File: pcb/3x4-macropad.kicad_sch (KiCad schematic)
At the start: 47 parts, among them SW1 SW_Push, SW10 SW_Push, SW11 SW_Push, SW12 SW_Push, SW2 SW_Push, SW3 SW_Push, SW4 SW_Push, SW5 SW_Push, SW6 SW_Push, SW7 SW_Push, SW8 SW_Push, SW9 SW_Push, U1 WeAct-RP2040-Pico

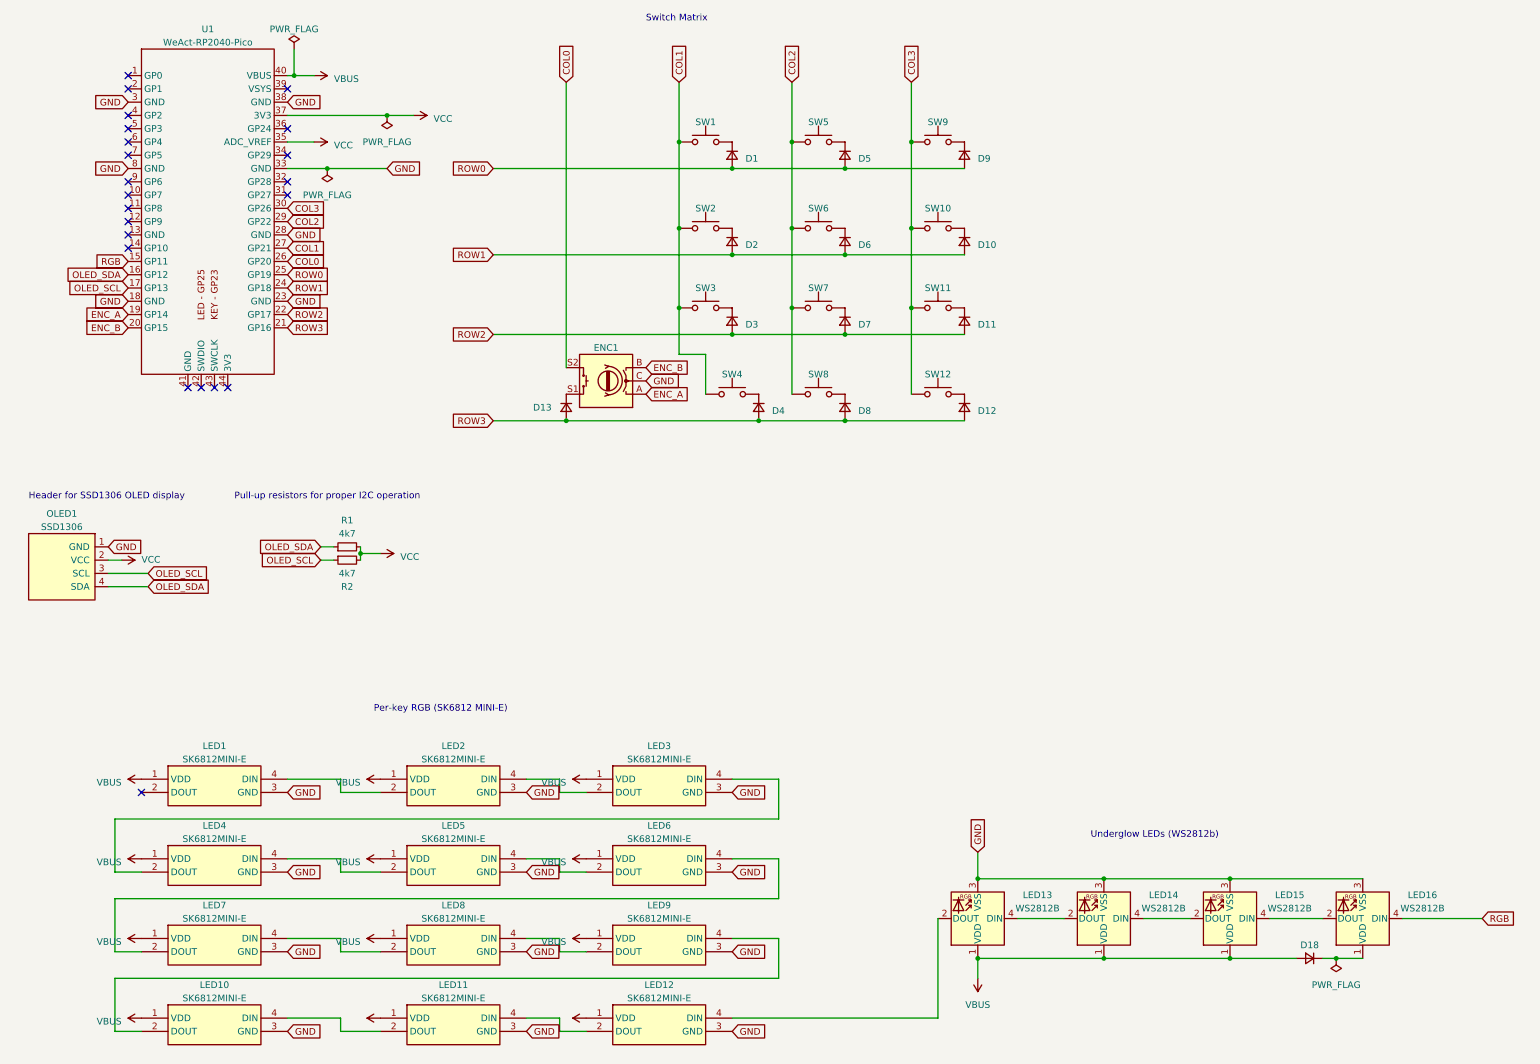
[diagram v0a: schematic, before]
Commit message: stuff
- cleaned up routing
- changed per-key rgb footprint
- changed resistor footprint
- changed diode footprint to actually support sod123
- made power traces 0.5mm
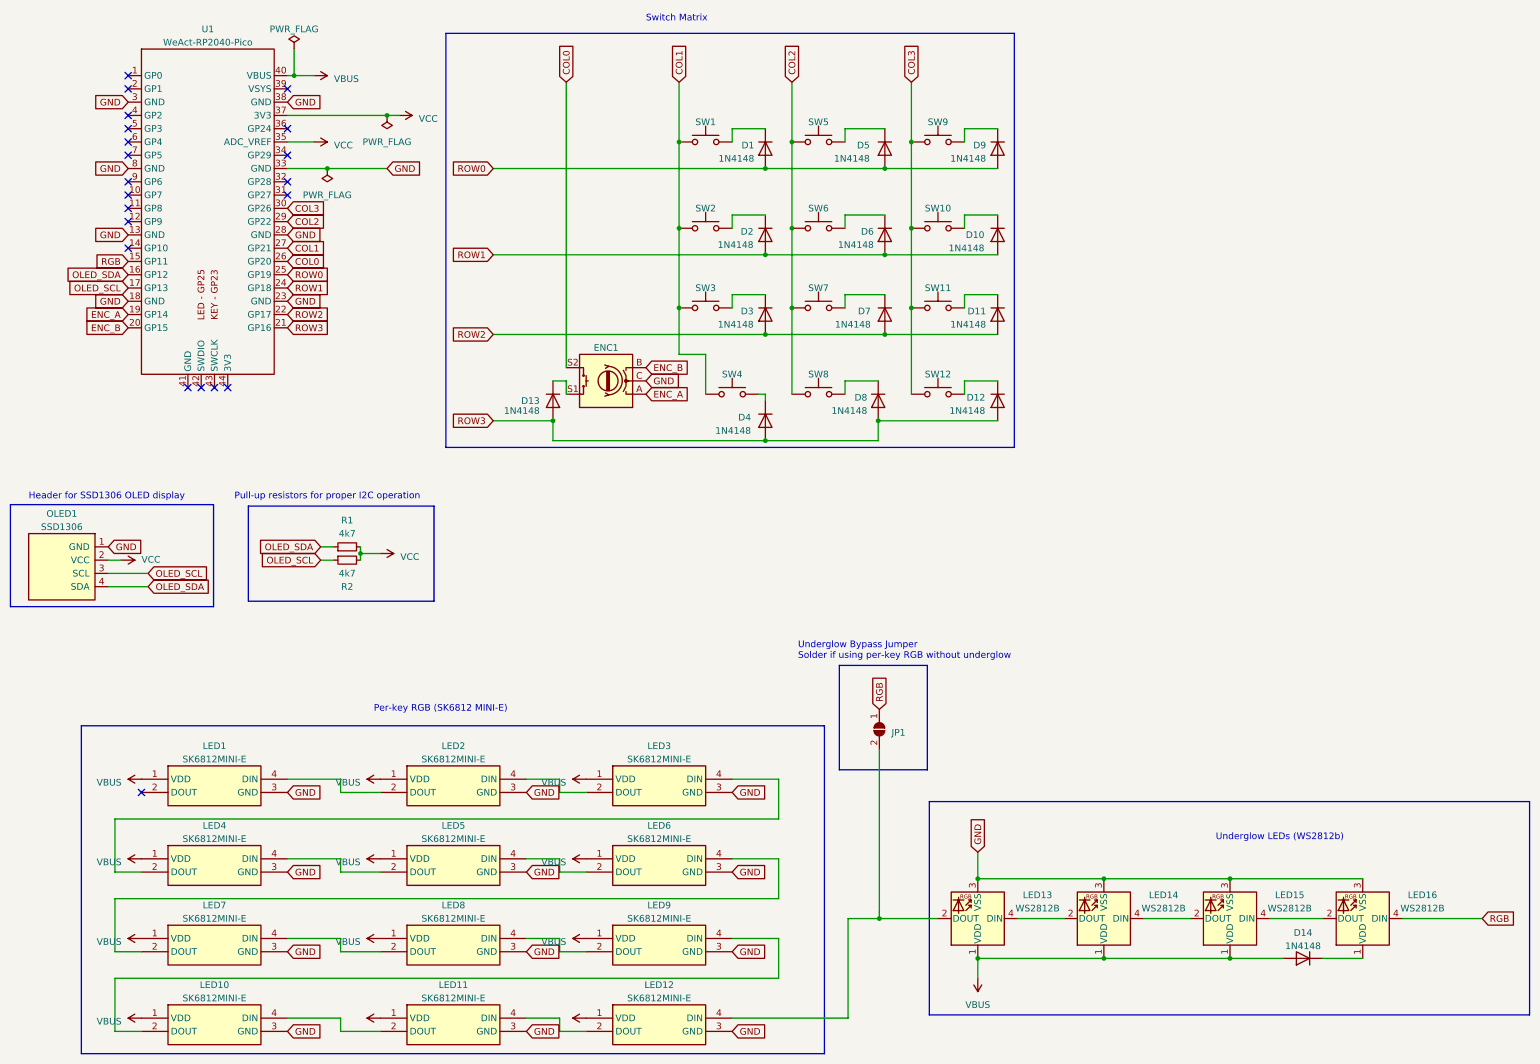
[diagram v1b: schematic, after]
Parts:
- removed D1, D10, D11, D12, D13, D18, D2, D3, D4, D5, D6, D7, D8, D9: D_Small, Keebio-Parts:Diode-dual, symbol Device:D_Small
- added D1, D10, D11, D12, D13, D14, D2, D3, D4, D5, D6, D7, D8, D9: 1N4148, Keebio-Parts:Diode-Hybrid-Back, symbol Diode:1N4148
- added JP1: SolderJumper_2_Open, Jumper:SolderJumper-2_P1.3mm_Open_RoundedPad1.0x1.5mm, symbol Jumper:SolderJumper_2_Open
- LED1, LED10, LED11, LED12, LED2, LED3, LED4, LED5, LED6, LED7, LED8, LED9: footprint SK6812MINI-E:SK6812MINIE -> Keebio-Parts:SK6812-MINI-E
- LED13, LED14, LED15, LED16: footprint LED_SMD:LED_WS2812B_PLCC4_5.0x5.0mm_P3.2mm -> Keebio-Parts:WS2812B
- R1, R2: footprint Resistor_THT:R_Axial_DIN0204_L3.6mm_D1.6mm_P5.08mm_Horizontal -> Keebio-Parts:Resistor-Hybrid
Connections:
- net GND: now also U1.13 (GND)
- net RGB: now also JP1.1 (A)
- net ROW0: now also D1.2 (A), D5.2 (A), D9.2 (A)
- net ROW1: now also D10.2 (A), D2.2 (A), D6.2 (A)
- net ROW2: now also D11.2 (A), D3.2 (A), D7.2 (A)
- net ROW3: now also D12.2 (A), D13.2 (A), D4.2 (A), D8.2 (A)
- net VBUS: now also D14.2 (A)
- net at SW10.2: now also D10.1 (K)
- net at SW6.2: now also D6.1 (K)
- net at SW12.2: now also D12.1 (K)
- net at SW1.2: now also D1.1 (K)
- net at SW3.2: now also D3.1 (K)
- net at SW5.2: now also D5.1 (K)
- net at SW7.2: now also D7.1 (K)
- net at SW2.2: now also D2.1 (K)
- net at SW11.2: now also D11.1 (K)
- net at SW4.2: now also D4.1 (K)
- net at SW9.2: now also D9.1 (K)
- net at LED16.1 (VDD): now also D14.1 (K)
- net at LED12.4 (DIN), LED13.2 (DOUT): now also JP1.2 (B)
- net at ENC1.S1: now also D13.1 (K)
- net at SW8.2: now also D8.1 (K)
- no-connect marks 22 -> 21
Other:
- note added: "Underglow Bypass Jumper Solder if using per-key RGB without underglow"

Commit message: Init rp2040 on board
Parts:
- removed U1: WeAct-RP2040-Pico, WeAct-RP2040-Pico:WeAct-RP2040-Pico, symbol WeAct-RP2040-Pico:WeAct-RP2040-Pico
- added C1, C16: 10u, Capacitor_SMD:C_0805_2012Metric, symbol Device:C_Small
- added C10, C2: 1u, Capacitor_SMD:C_0402_1005Metric, symbol Device:C_Small
- added C11, C12, C13, C3, C4, C5, C6, C7, C8, C9: 100n, Capacitor_SMD:C_0402_1005Metric, symbol Device:C_Small
- added C14, C15: 27pF, Capacitor_SMD:C_0402_1005Metric, symbol Device:C_Small
- added J2: Conn_01x02, Keebio-Parts:SW_Tactile_SPST_Angled_MJTP1117, symbol Connector_Generic:Conn_01x02
- added J3: Conn_01x02, Connector_PinHeader_1.00mm:PinHeader_1x02_P1.00mm_Vertical, symbol Connector_Generic:Conn_01x02
- added J4: USB_C_Receptacle_USB2.0, Connector_USB:USB_C_Receptacle_HRO_TYPE-C-31-M-12, symbol Connector:USB_C_Receptacle_USB2.0
- added R10, R7, R9: 1k, Resistor_SMD:R_0402_1005Metric, symbol Device:R_Small
- added R3, R4: 5k1, Resistor_SMD:R_0805_2012Metric, symbol Device:R_Small
- added R5, R6: 27.4, Resistor_SMD:R_0402_1005Metric, symbol Device:R_Small
- added R8: DNF(10k), Resistor_SMD:R_0402_1005Metric, symbol Device:R_Small
- added U1: RP2040, RP2040_minimal:RP2040-QFN-56, symbol MCU_RaspberryPi_RP2040:RP2040
- added U2: NCP1117-3.3_SOT223, Package_TO_SOT_SMD:SOT-223-3_TabPin2, symbol Regulator_Linear:NCP1117-3.3_SOT223
- added U3: W25Q32JVSS, Package_SO:SOIC-8_5.23x5.23mm_P1.27mm, symbol Memory_Flash:W25Q32JVSS
- added Y1: ABLS_12.000MHZ-B4-T, RP2040_minimal:Crystal_SMD_HC49-US, symbol Device:Crystal_Small
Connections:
- net COL0: now also U1.31 (GPIO20)
- net COL1: now also U1.32 (GPIO21)
- net COL2: now also U1.34 (GPIO22)
- net COL3: now also U1.38 (GPIO26_ADC0)
- net ENC_A: now also U1.17 (GPIO14)
- net ENC_B: now also U1.18 (GPIO15)
- net OLED_SCL: now also U1.16 (GPIO13)
- net OLED_SDA: now also U1.15 (GPIO12)
- net RGB: now also U1.14 (GPIO11)
- net ROW0: now also U1.30 (GPIO19)
- net ROW1: now also U1.29 (GPIO18)
- net ROW2: now also U1.28 (GPIO17)
- net ROW3: now also U1.27 (GPIO16)
- net VBUS: now also C1.1, J4.A4 (VBUS), J4.A9 (VBUS), J4.B4 (VBUS), J4.B9 (VBUS), U2.3 (VI)
- net GND renamed GND1
- net GND1: now also C1.2, C10.2, C11.2, C12.2, C13.2, C14.1, C15.1, C16.2, C2.2, C3.2, C4.2, C5.2, C6.2, C7.2, C8.2, C9.2, J2.2 (Pin_2), J4.A1 (GND), J4.A12 (GND), J4.B1 (GND), J4.B12 (GND), J4.S1 (SHIELD), R3.2, R4.2, U1.19 (TESTEN), U1.57 (GND), U2.1 (GND), U3.4 (GND)
- net VCC renamed +3V3
- net +3V3: now also C13.1, C16.1, C2.1, C3.1, C4.1, C5.1, C6.1, C7.1, C8.1, C9.1, R10.2, R8.1, U1.1 (IOVDD), U1.10 (IOVDD), U1.22 (IOVDD), U1.33 (IOVDD), U1.42 (IOVDD), U1.43 (ADC_AVDD), U1.44 (VREG_IN), U1.48 (USB_VDD), U1.49 (IOVDD), U2.2 (VO), U3.8 (VCC)
- new net: J4.A5 (CC1), R3.1
- new net: C14.2, R9.1, Y1.1
- new net: C15.2, U1.20 (XIN), Y1.2
- new net: R6.1, U1.46 (USB_DM)
- new net: R9.2, U1.21 (XOUT)
- new net: R10.1, U1.26 (RUN)
- new net: R5.1, U1.47 (USB_DP)
- new net: J4.B5 (CC2), R4.1
- new net +1V1: C10.1, C11.1, C12.1, U1.23 (DVDD), U1.45 (VREG_VOUT), U1.50 (DVDD)
- new net QSPI_SCLK: U1.52 (QSPI_SCLK), U3.6 (CLK)
- new net QSPI_SD0: U1.53 (QSPI_SD0), U3.5 (DI(IO0))
- new net QSPI_SD1: U1.55 (QSPI_SD1), U3.2 (DO(IO1))
- new net QSPI_SD2: U1.54 (QSPI_SD2), U3.3 (IO2)
- new net QSPI_SD3: U1.51 (QSPI_SD3), U3.7 (IO3)
- new net QSPI_SS: R7.1, R8.2, U1.56 (QSPI_SS), U3.1 (~{CS})
- new net SWCLK: J3.1 (Pin_1), U1.24 (SWCLK)
- new net SWD: J3.2 (Pin_2), U1.25 (SWD)
- new net USB_BOOT: J2.1 (Pin_1), R7.2
- new net USB_D+: J4.A6 (D+), J4.B6 (D+), R5.2
- new net USB_D-: J4.A7 (D-), J4.B7 (D-), R6.2
- no-connect marks 21 -> 20
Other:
- note added: "Make sure C10 is close to pin 45 of RP2040"
- note added: "Make sure C2 is close to pin 44 of RP2040"
- note added: "Power supply to RP2040"
